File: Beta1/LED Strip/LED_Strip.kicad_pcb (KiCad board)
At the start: 2 copper layers, 194 x 16.1 mm, 212 parts, among them U0 APA102C, U1 APA102C, U10 APA102C, U11 APA102C, U12 APA102C, U13 APA102C, U14 APA102C, U15 APA102C, U16 APA102C, U17 APA102C, U18 APA102C, U19 APA102C, U2 APA102C, U20 APA102C, U21 APA102C, U22 APA102C, U23 APA102C, U24 APA102C, U25 APA102C, U26 APA102C, U27 APA102C, U28 APA102C, U29 APA102C, U3 APA102C, U30 APA102C, U31 APA102C, U32 SN74LV1T125DBVR, U33 SN74LVC2T45DCTT, U4 APA102C, U5 APA102C, U6 APA102C, U7 APA102C, U8 APA102C, U9 APA102C

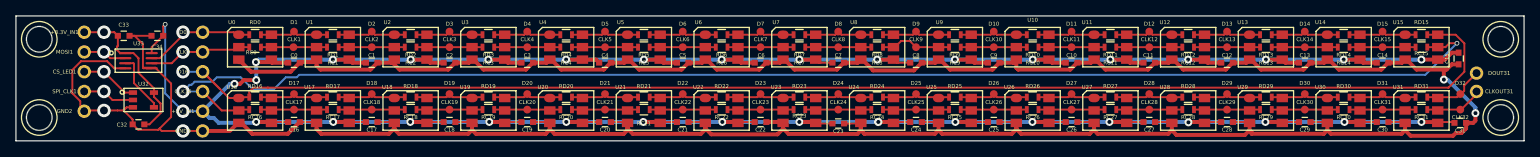
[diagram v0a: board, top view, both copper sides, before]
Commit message: Converted vias to plated through holes. Vias are / can be tented over.
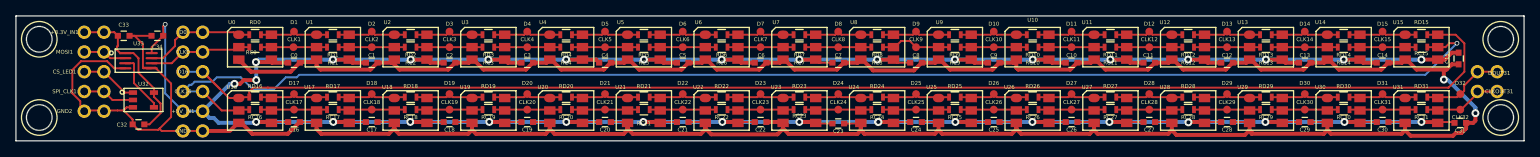
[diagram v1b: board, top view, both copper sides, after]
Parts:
- added +3.3V_INB1: CONN_01X01, Liberry:single_0.1, F.Cu at (11.3, -14.0)
- added +5V_INB1: CONN_01X01, Liberry:single_0.1, F.Cu at (21.5, -3.81)
- added CLKB0: CONN_01X01, Liberry:single_0.1, F.Cu at (21.5, -11.4)
- added CLKB16: CONN_01X01, Liberry:single_0.1, F.Cu at (21.5, -6.35)
- added CLKOUTB31: CONN_01X01, Liberry:single_0.1, F.Cu at (190.4, -6.35)
- added CS_LEDB1: CONN_01X01, Liberry:single_0.1, F.Cu at (11.3, -8.89)
- added DB0: CONN_01X01, Liberry:single_0.1, F.Cu at (21.5, -14.0)
- added DB16: CONN_01X01, Liberry:single_0.1, F.Cu at (21.5, -8.89)
- added DOUTB31: CONN_01X01, Liberry:single_0.1, F.Cu at (190.4, -8.89)
- added GNDB0: CONN_01X01, Liberry:single_0.1, F.Cu at (21.5, -1.27)
- added GNDB2: CONN_01X01, Liberry:single_0.1, F.Cu at (11.3, -3.81)
- added MOSIB1: CONN_01X01, Liberry:single_0.1, F.Cu at (11.3, -11.4)
- added SPI_CLKB1: CONN_01X01, Liberry:single_0.1, F.Cu at (11.3, -6.35)
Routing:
- net /D32: track 8.08 -> 10.9 mm
- net /CLK32: track 7.56 -> 10.1 mm
- net Net-(SPI_CLK1-Pad1): track 7.25 -> 6.72 mm, vias 1 -> 0
- net Net-(D0-Pad1): track 14.4 -> 14.6 mm, vias 1 -> 0
- net Net-(MOSI1-Pad1): vias 1 -> 0
- net Net-(CS_LED1-Pad1): vias 1 -> 0
- net Net-(CLK0-Pad1): vias 1 -> 0
- net GND: vias 4 -> 2
- net /D16: vias 1 -> 0
- net /CLK16: vias 2 -> 1
- net +5V: vias 36 -> 35
- net +3V3: vias 1 -> 0

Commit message: Added PCB# and Flavortext
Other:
- board text added: "PCBBTWL_LED32-Beta1 2016-11-18 Believotron Wanderlust 32CH Serial RGB APA102C LED Array of dazzling light. Light is truth. Use it to cast different perspectives and learn more, ever more truth."
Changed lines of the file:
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@@
   (general
     (links 418)
-    (no_connects 2)
+    (no_connects 0)
     (area -0.050001 -16.112501 194.010001 0.050001)
     (thickness 1.6)
-    (drawings 13)
+    (drawings 14)
     (tracks 864)
     (zones 0)
@@
       (net 36 /D16))
   )
+  (gr_text "PCBBTWL_LED32-Beta1 2016-11-18 Believotron Wanderlust 32CH Serial RGB APA102C LED Array of dazzling light. Light is truth. Use it to cast different perspectives and learn more, ever more truth.\n" (at 32.656 -8.128) (layer F.SilkS)
+    (effects (font (size 0.5 0.5) (thickness 0.125)) (justify left))
+  )
   (gr_line (start 165.76 0) (end 165.76 -15.625) (layer Dwgs.User) (width 0.2))

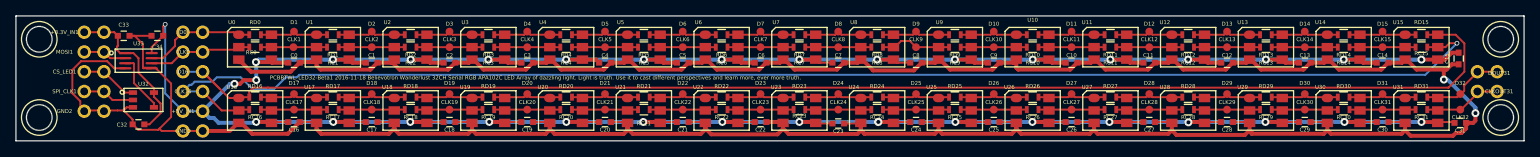
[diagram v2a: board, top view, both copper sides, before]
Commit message: Catchup Commit.  Non-atomic, Refactored LED, Keyboard, KeyPAD, and Knobs PCBs
LED: Changed chips. Cleaned up silkscreen text. Added some support
mounting holes. Shrank height of board to avoid stackup. KeyPAD is
updated with new footprint. Keyboard and Knobs are unknown.
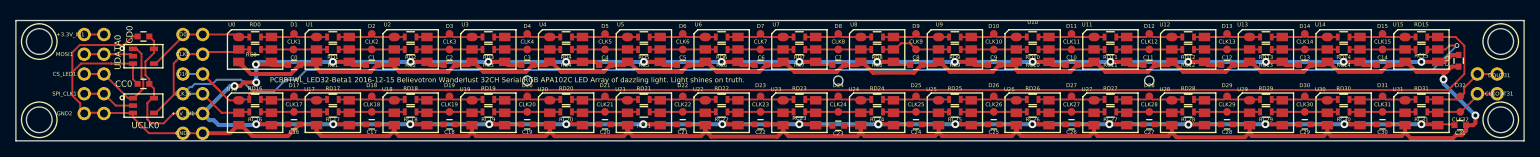
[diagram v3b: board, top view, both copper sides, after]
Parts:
- removed C32, C33, C34: 0.1u, Capacitors_SMD:C_0603
- removed U32: SN74LV1T125DBVR, Liberry:SOT23-5
- removed U33: SN74LVC2T45DCTT, Liberry:SSOP8
- added CC0: 0.1u, Capacitors_SMD:C_0603, F.Cu at (16.4, -7.33)
- added CD0: 0.1u, Capacitors_SMD:C_0603, F.Cu at (16.4, -13.4)
- added REF**: 1pin, Connect:1pin, B.Cu at (145.8, -7.74)
- added REF**: 1pin, Connect:1pin, B.Cu at (65.8, -7.74)
- added REF**: 1pin, Connect:1pin, B.Cu at (105.8, -7.74)
- added UCLK0: SN74LV1T125DBVR, Liberry:SOT23-5, F.Cu at (16.4, -4.53)
- added UDATA0: SN74LV1T125DBVR, Liberry:SOT23-5, F.Cu at (16.4, -10.9)
- moved +3.3V_IN1 0.29 mm to (8.78, -13.7)
- moved +3.3V_INB1 0.29 mm to (11.3, -13.7)
- moved C0 0.29 mm to (35.8, -9.75)
- moved C1 0.29 mm to (45.8, -9.75)
- moved C10 0.29 mm to (135.8, -9.75)
- moved C11 0.29 mm to (145.8, -9.75)
- moved C12 0.29 mm to (155.8, -9.75)
- moved C13 0.29 mm to (165.8, -9.75)
- moved C14 0.29 mm to (175.8, -9.75)
- moved C2 0.29 mm to (55.8, -9.75)
- moved C3 0.29 mm to (65.8, -9.75)
- moved C4 0.29 mm to (75.8, -9.75)
- moved C5 0.29 mm to (85.8, -9.75)
- moved C6 0.29 mm to (95.8, -9.75)
- moved C7 0.29 mm to (105.8, -9.75)
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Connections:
- net Net-(CLK0-Pad1) renamed /CLK
- net Net-(D0-Pad1) renamed /Data
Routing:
- net +3V3: track 20.6 -> 2.54 mm
- net Net-(CS_LED1-Pad1): track 7.38 -> 15.4 mm
- net Net-(U32-Pad4): track 7.82 -> 0.00 mm
- net GND: track 462.9 -> 456.4 mm
- net /CLK: track 13.5 -> 18.1 mm
- net +5V: track 477.8 -> 478.8 mm, vias 35 -> 34
- net Net-(MOSI1-Pad1): track 5.61 -> 6.38 mm
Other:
- board size 194 x 16.1 mm -> 194 x 15.5 mm
- board text added: "PCBBTWL_LED32-Beta1 2016-12-15 Believotron Wanderlust 32CH Serial RGB APA102C LED Array of dazzling light. Light shines on truth."
- board text removed: "PCBBTWL_LED32-Beta1 2016-11-18 Believotron Wanderlust 32CH Serial RGB APA102C LED Array of dazzling light. Light is truth. Use it to cast different perspectives and learn more, ever more truth."
